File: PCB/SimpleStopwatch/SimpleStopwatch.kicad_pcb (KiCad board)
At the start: 2 copper layers, 85 x 30 mm, 36 parts, among them J1 Switch, J2 + Power -, U1 TPS5430DDA, U2 ATmega328P-AU, U3 ULN2003, Y1 Crystal_Small

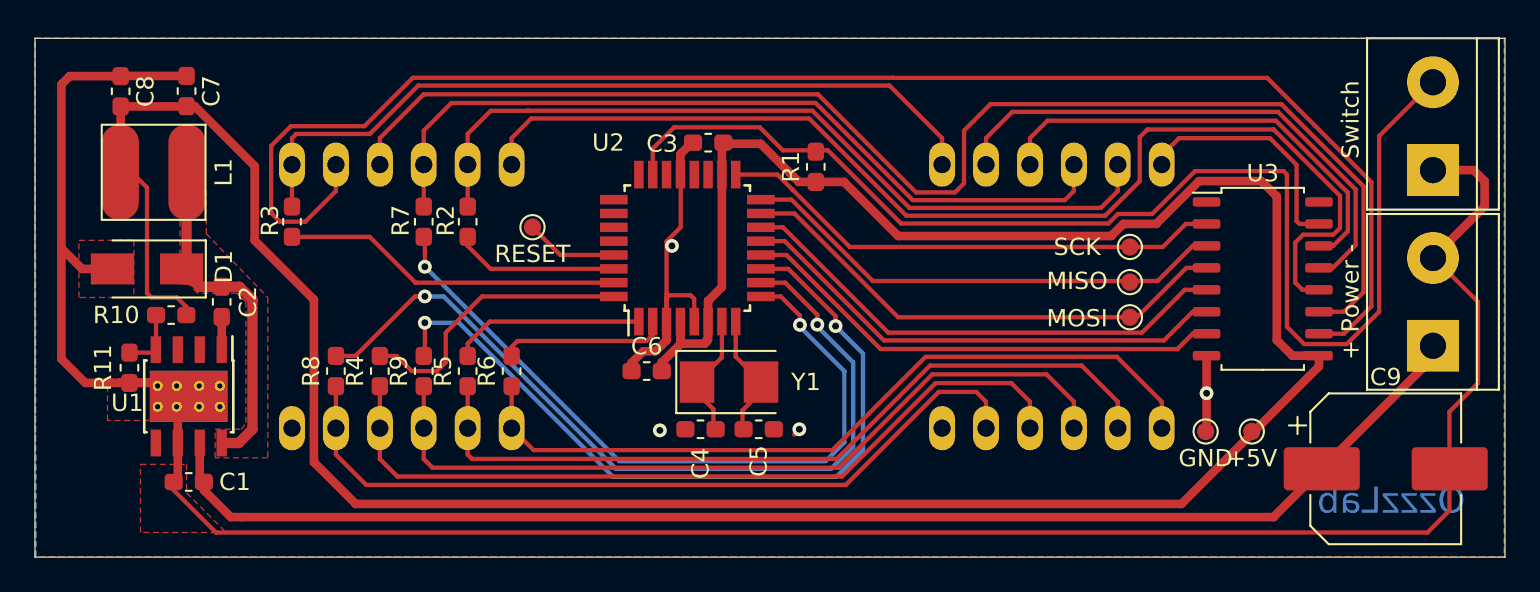
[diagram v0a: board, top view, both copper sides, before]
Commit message: PCB Changes. Size of capacitors
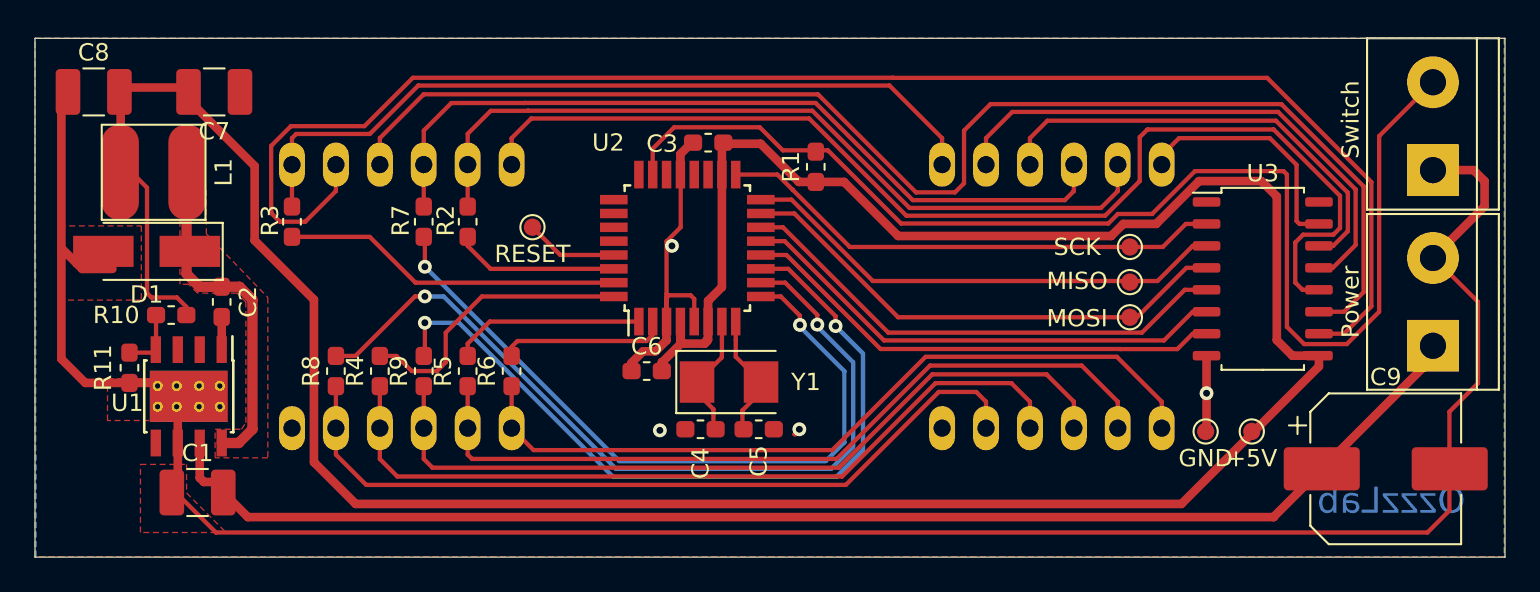
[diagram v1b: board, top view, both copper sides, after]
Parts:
- C1, C7, C8: footprint Capacitor_SMD:C_0603_1608Metric_Pad1.05x0.95mm_HandSolder -> Capacitor_SMD:C_1210_3225Metric_Pad1.42x2.65mm_HandSolder
- D1: footprint Diode_SMD:D_SMA -> Diode_SMD:D_SMA_Handsoldering
- J2: value + Power - -> Power
- R10: value 1k -> 5.1k
- R11: value 1k -> 1.8k
- moved C7 1.60 mm to (10.4, 3.10), turned to 180 degrees
- moved C8 1.56 mm to (3.39, 3.10), turned to 0 degrees
- moved D1 1.02 mm to (6.45, 12.3)
- moved C1 0.79 mm to (9.40, 26.3)
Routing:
- net GND: track 164.2 -> 157.4 mm
- net +5V: track 170.7 -> 173.0 mm
